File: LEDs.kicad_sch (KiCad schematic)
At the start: 27 parts

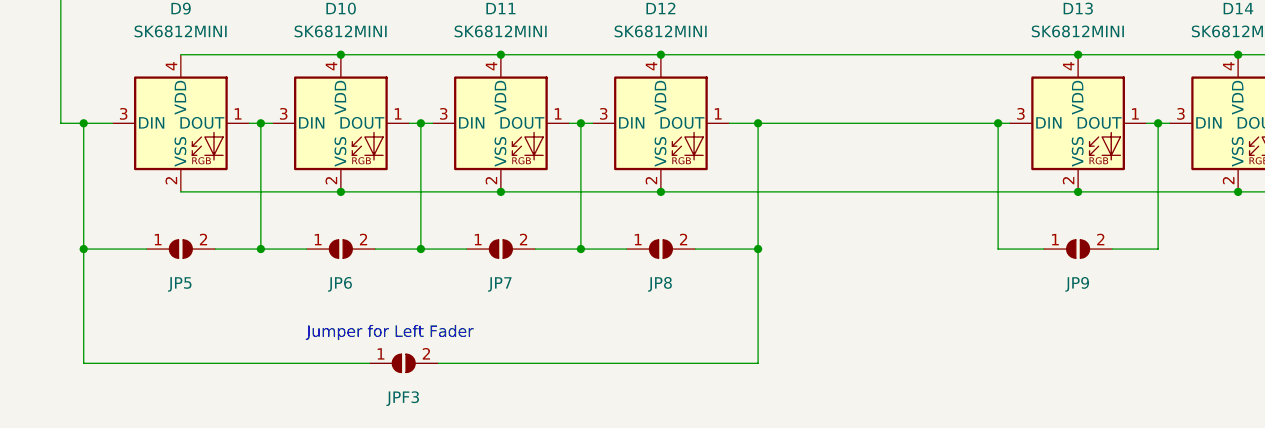
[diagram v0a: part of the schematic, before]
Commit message: updated libs, positioned jumpers
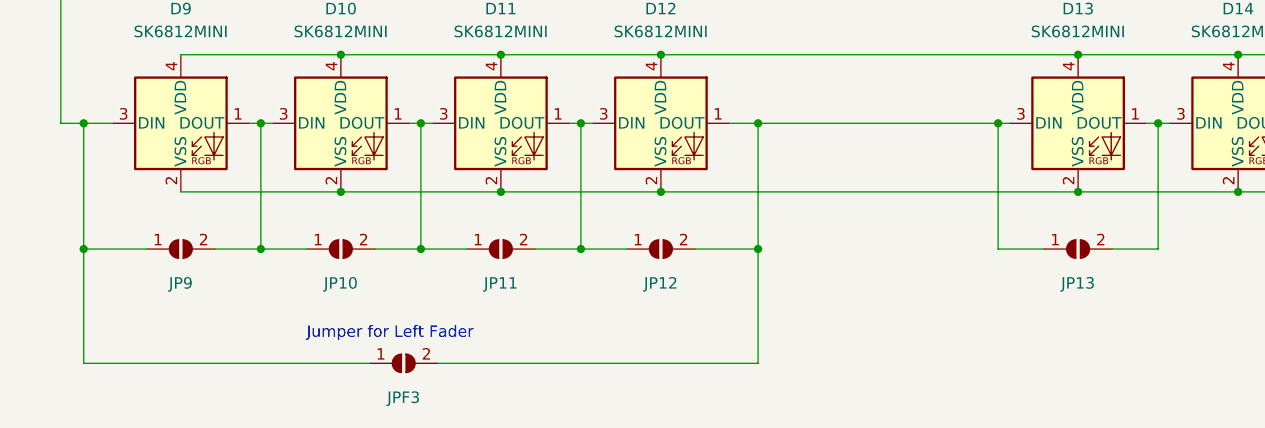
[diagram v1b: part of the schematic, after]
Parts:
- renumbered JP6 to JP10, JP7 to JP11, JP8 to JP12, JP9 to JP13, JP5 to JP9
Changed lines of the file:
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@@
   (symbol (lib_id "Jumper:SolderJumper_2_Open") (at 118.745 143.51 0) (unit 1)
     (in_bom yes) (on_board yes)
-    (property "Reference" "JP7" (id 0) (at 118.745 147.32 0))
+    (property "Reference" "JP11" (id 0) (at 118.745 147.32 0))
     (property "Value" "SolderJumper_2_Open" (id 1) (at 118.745 149.86 0)
       (effects (font (size 1.27 1.27)) hide)
@@
   (symbol (lib_id "Jumper:SolderJumper_2_Open") (at 182.88 143.51 0) (unit 1)
     (in_bom yes) (on_board yes)
-    (property "Reference" "JP9" (id 0) (at 182.88 147.32 0))
+    (property "Reference" "JP13" (id 0) (at 182.88 147.32 0))
     (property "Value" "SolderJumper_2_Open" (id 1) (at 182.88 149.86 0)
       (effects (font (size 1.27 1.27)) hide)
@@
   (symbol (lib_id "Jumper:SolderJumper_2_Open") (at 83.185 143.51 0) (unit 1)
     (in_bom yes) (on_board yes)
-    (property "Reference" "JP5" (id 0) (at 83.185 147.32 0))
+    (property "Reference" "JP9" (id 0) (at 83.185 147.32 0))
     (property "Value" "SolderJumper_2_Open" (id 1) (at 83.185 149.86 0)
       (effects (font (size 1.27 1.27)) hide)
@@
   (symbol (lib_id "Jumper:SolderJumper_2_Open") (at 136.525 143.51 0) (unit 1)
     (in_bom yes) (on_board yes)
-    (property "Reference" "JP8" (id 0) (at 136.525 147.32 0))
+    (property "Reference" "JP12" (id 0) (at 136.525 147.32 0))
     (property "Value" "SolderJumper_2_Open" (id 1) (at 136.525 149.86 0)
       (effects (font (size 1.27 1.27)) hide)
@@
   (symbol (lib_id "Jumper:SolderJumper_2_Open") (at 100.965 143.51 0) (unit 1)
     (in_bom yes) (on_board yes)
-    (property "Reference" "JP6" (id 0) (at 100.965 147.32 0))
+    (property "Reference" "JP10" (id 0) (at 100.965 147.32 0))
     (property "Value" "SolderJumper_2_Open" (id 1) (at 100.965 149.86 0)
       (effects (font (size 1.27 1.27)) hide)

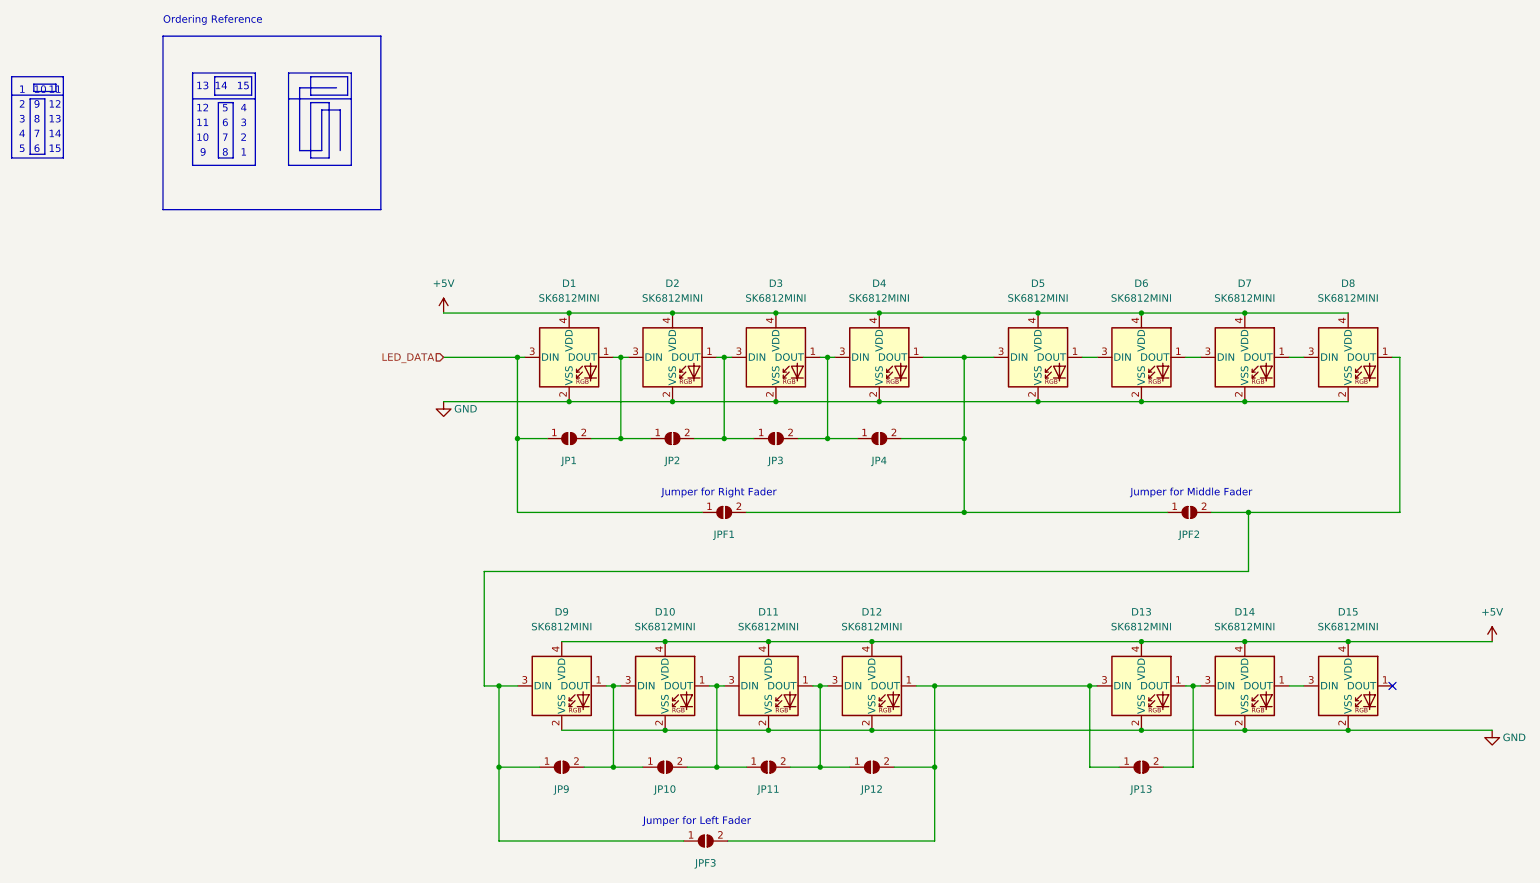
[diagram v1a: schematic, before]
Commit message: Centered faders and rotated LEDs
Experimental solution to make faders centered to lower 4 rows of keys/grid. Requires bending or trimming off an unused pin from the faders.
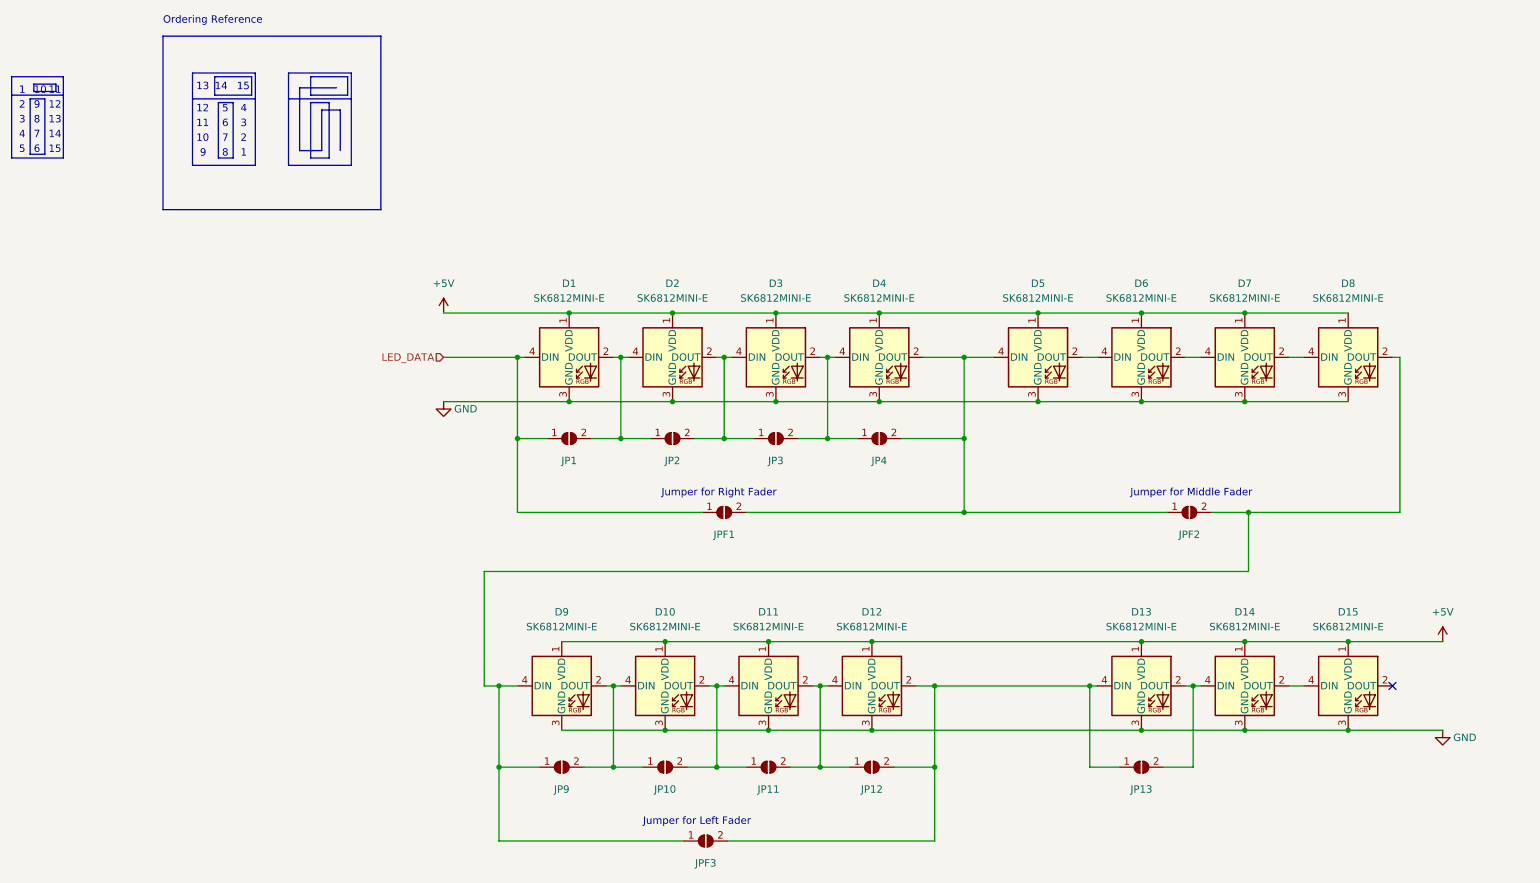
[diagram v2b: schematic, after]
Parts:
- D1, D10, D11, D12, D13, D14, D15, D2, D3, D4, D5, D6, D7, D8, D9: value SK6812MINI -> SK6812MINI-E; footprint marbastlib-mx:LED_MX_6028R_lower-offset -> Keeby-Cat Footprints:LED_MX_SK6812MINI-E; symbol LED:SK6812MINI -> keeby-cat-symbols:SK6812MINI-E
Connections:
- net +5V: now also D1.1 (VDD), D10.1 (VDD), D11.1 (VDD), D12.1 (VDD), D13.1 (VDD), D14.1 (VDD), D15.1 (VDD), D2.1 (VDD), D3.1 (VDD), D4.1 (VDD), D5.1 (VDD), D6.1 (VDD), D7.1 (VDD), D8.1 (VDD), D9.1 (VDD); no longer D1.4 (VDD), D10.4 (VDD), D11.4 (VDD), D12.4 (VDD), D13.4 (VDD), D14.4 (VDD), D15.4 (VDD), D2.4 (VDD), D3.4 (VDD), D4.4 (VDD), D5.4 (VDD), D6.4 (VDD), D7.4 (VDD), D8.4 (VDD), D9.4 (VDD)
- net GND: now also D1.3 (GND), D10.3 (GND), D11.3 (GND), D12.3 (GND), D13.3 (GND), D14.3 (GND), D15.3 (GND), D2.3 (GND), D3.3 (GND), D4.3 (GND), D5.3 (GND), D6.3 (GND), D7.3 (GND), D8.3 (GND), D9.3 (GND); no longer D1.2 (VSS), D10.2 (VSS), D11.2 (VSS), D12.2 (VSS), D13.2 (VSS), D14.2 (VSS), D15.2 (VSS), D2.2 (VSS), D3.2 (VSS), D4.2 (VSS), D5.2 (VSS), D6.2 (VSS), D7.2 (VSS), D8.2 (VSS), D9.2 (VSS)
- net LED_DATA: now also D1.4 (DIN); no longer D1.3 (DIN)
- net at JP1.2 (B), JP2.1 (A): now also D1.2 (DOUT), D2.4 (DIN); no longer D1.1 (DOUT), D2.3 (DIN)
- net at JP2.2 (B), JP3.1 (A): now also D2.2 (DOUT), D3.4 (DIN); no longer D2.1 (DOUT), D3.3 (DIN)
- net at JP9.1 (A), JPF2.2 (B), JPF3.1 (A): now also D8.2 (DOUT), D9.4 (DIN); no longer D8.1 (DOUT), D9.3 (DIN)
- net at JP10.2 (B), JP11.1 (A): now also D10.2 (DOUT), D11.4 (DIN); no longer D10.1 (DOUT), D11.3 (DIN)
- net at JP11.2 (B), JP12.1 (A): now also D11.2 (DOUT), D12.4 (DIN); no longer D11.1 (DOUT), D12.3 (DIN)
- net at JP12.2 (B), JP13.1 (A), JPF3.2 (B): now also D12.2 (DOUT), D13.4 (DIN); no longer D12.1 (DOUT), D13.3 (DIN)
- net at JP10.1 (A), JP9.2 (B): now also D10.4 (DIN), D9.2 (DOUT); no longer D10.3 (DIN), D9.1 (DOUT)
- net at JP3.2 (B), JP4.1 (A): now also D3.2 (DOUT), D4.4 (DIN); no longer D3.1 (DOUT), D4.3 (DIN)
- net at JP4.2 (B), JPF1.2 (B), JPF2.1 (A): now also D4.2 (DOUT), D5.4 (DIN); no longer D4.1 (DOUT), D5.3 (DIN)
- new net: D7.2 (DOUT), D8.4 (DIN)
- new net: D6.2 (DOUT), D7.4 (DIN)
- new net: D5.2 (DOUT), D6.4 (DIN)
- new net: D13.2 (DOUT), D14.4 (DIN), JP13.2 (B)
- new net: D14.2 (DOUT), D15.4 (DIN)

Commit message: routing improvements
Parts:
- D12, D4, D5: footprint Keeby-Cat Footprints:LED_MX_SK6812MINI-E -> Keeby-Cat Footprints:LED_MX_SK6812MINI-E_rotated
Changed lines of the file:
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@@
     (property "Reference" "D12" (id 0) (at 136.525 116.84 0))
     (property "Value" "SK6812MINI-E" (id 1) (at 136.525 119.38 0))
-    (property "Footprint" "Keeby-Cat Footprints:LED_MX_SK6812MINI-E" (id 2) (at 136.525 104.14 0)
+    (property "Footprint" "Keeby-Cat Footprints:LED_MX_SK6812MINI-E_rotated" (id 2) (at 136.525 104.14 0)
       (effects (font (size 1.27 1.27)) (justify top) hide)
     )
@@
     (property "Reference" "D4" (id 0) (at 137.795 60.325 0))
     (property "Value" "SK6812MINI-E" (id 1) (at 137.795 62.865 0))
-    (property "Footprint" "Keeby-Cat Footprints:LED_MX_SK6812MINI-E" (id 2) (at 137.795 47.625 0)
+    (property "Footprint" "Keeby-Cat Footprints:LED_MX_SK6812MINI-E_rotated" (id 2) (at 137.795 47.625 0)
       (effects (font (size 1.27 1.27)) (justify top) hide)
     )
@@
     (property "Reference" "D5" (id 0) (at 165.1 60.325 0))
     (property "Value" "SK6812MINI-E" (id 1) (at 165.1 62.865 0))
-    (property "Footprint" "Keeby-Cat Footprints:LED_MX_SK6812MINI-E" (id 2) (at 165.1 47.625 0)
+    (property "Footprint" "Keeby-Cat Footprints:LED_MX_SK6812MINI-E_rotated" (id 2) (at 165.1 47.625 0)
       (effects (font (size 1.27 1.27)) (justify top) hide)
     )
